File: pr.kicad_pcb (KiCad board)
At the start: 2 copper layers, 65 x 86 mm, 42 parts, among them P1 CONN_01X02, P2 CONN_01X02, P4 BDM, P5 CONN_01X03, P6 CONN_01X02, T1 TRANSFO, U1 78L05, U2 MC9S08SH8, U4 LM311N, U5 SSR_SHARP

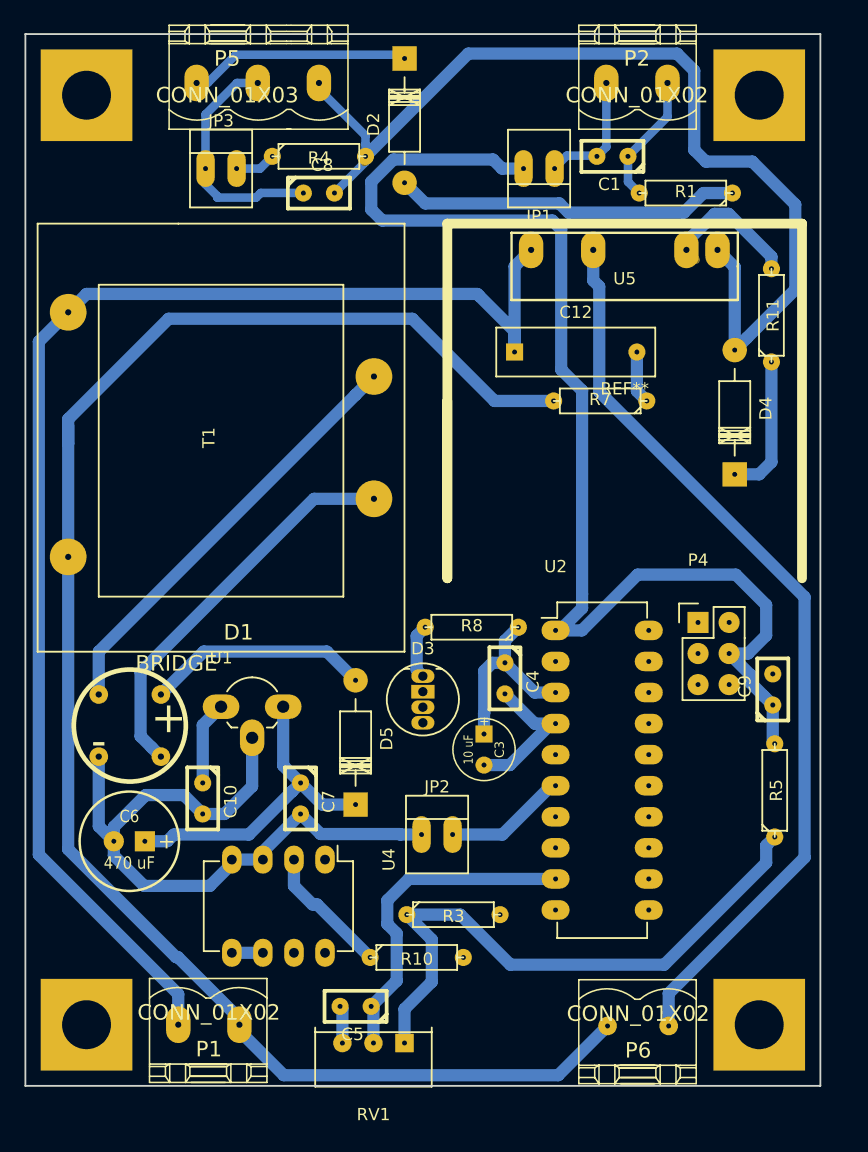
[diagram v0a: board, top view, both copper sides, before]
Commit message: modificado componente ruteado
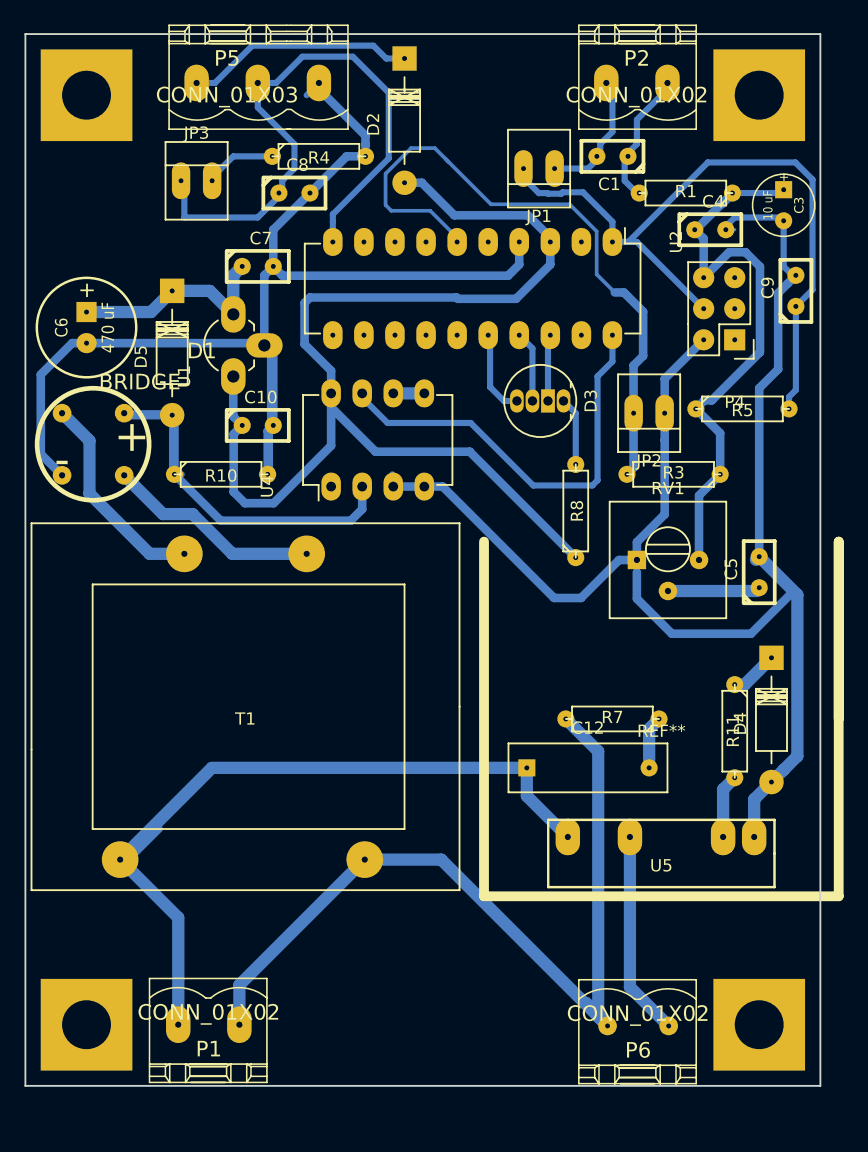
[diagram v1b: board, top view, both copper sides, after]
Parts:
- RV1: footprint Potentiometers:Potentiometer_Trimmer-Suntan-TSR-3386C -> Potentiometers:Potentiometer_Trimmer-Suntan-TSR-3386P
- moved C3 50.8 mm to (106.0, 64.0)
- moved C5 48.5 mm to (104.0, 94.0), turned to 90 degrees
- moved U5 48.1 mm to (96.0, 117.0)
- moved D5 44.6 mm to (56.0, 71.0), turned to 270 degrees
- moved RV1 43.8 mm to (94.0, 93.0), turned to 0 degrees
- moved C7 43.6 mm to (63.0, 69.0), turned to 0 degrees
- moved R10 42.6 mm to (60.0, 86.0)
- moved C6 42.1 mm to (49.0, 74.0), turned to 270 degrees
- moved C4 40.3 mm to (100.0, 66.0), turned to 0 degrees
- moved R3 40.2 mm to (97.0, 86.0), turned to 180 degrees
- moved JP2 38.6 mm to (95.0, 81.0), turned to 180 degrees
- moved R11 34.1 mm to (102.0, 107.0), turned to 270 degrees
- moved C12 34.0 mm to (85.0, 110.0)
- moved C9 32.6 mm to (107.0, 71.0)
- moved U2 32.1 mm to (92.0, 67.0), turned to 270 degrees
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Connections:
- RV1 pad 1: /vreg -> GND
- RV1 pad 3: GND -> /vreg
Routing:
- net GND: track 155.9 -> 234.7 mm
- net /L: track 141.9 -> 65.7 mm
- net /N: track 136.5 -> 75.1 mm
- net Net-(P6-Pad1): track 75.3 -> 16.8 mm
- net /vreg: track 100.2 -> 146.7 mm
- net Net-(JP2-Pad2): track 10.1 -> 53.9 mm
- net /RESET: track 101.8 -> 61.4 mm
- net /ZC: track 0.35 -> 35.1 mm
- net Net-(C8-Pad1): track 19.9 -> 50.2 mm
- net /ST: track 27.4 -> 7.57 mm
- net Net-(D1-Pad2): track 35.3 -> 17.3 mm
- net Net-(D1-Pad4): track 32.5 -> 17.6 mm
- net /IZC: track 29.1 -> 38.8 mm
- net Net-(C6-Pad1): track 26.8 -> 17.7 mm
- net Net-(R11-Pad2): track 12.6 -> 5.23 mm
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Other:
- net class Default: trace_width 1 -> 0.7
- net class PW added: clearance 0.4, trace_width 0.7, via_dia 0.6, via_drill 0.4

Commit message: prototipo1.0 enviado a fabricar
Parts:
- added G***: LOGO, locales:LOGO, B.Cu at (76.0, 128.2)
- moved RV1 4.50 mm to (93.6, 97.5)
- moved D2 2.68 mm to (77.7, 52.0)
- moved R8 2.41 mm to (88.8, 91.4)
- moved REF** 1.61 mm to (94.5, 105.5)
- moved U5 1.52 mm to (94.5, 116.8)
- moved C8 1.42 mm to (67.1, 62.1)
- moved R5 1.14 mm to (103.8, 80.8)
- moved C6 1.02 mm to (50.0, 74.0)
- moved R4 0.81 mm to (67.9, 59.2)
- moved JP3 0.77 mm to (58.4, 61.4)
- moved D1 0.75 mm to (47.8, 81.0)
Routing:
- net /ST: track 7.57 -> 128.8 mm, vias 0 -> 4
- net /AcOut: track 5.10 -> 75.4 mm, vias 0 -> 2
- net /vreg: track 146.7 -> 176.5 mm, vias 0 -> 2
- net /BDM: track 0.03 -> 26.4 mm, vias 0 -> 2
- net GND: track 234.7 -> 260.0 mm, vias 0 -> 2
- net Net-(JP2-Pad2): track 53.9 -> 65.3 mm
- net /ZC: track 35.1 -> 43.9 mm
- net /L: track 65.7 -> 60.9 mm
- net Net-(D2-Pad1): track 18.7 -> 22.9 mm
- net Net-(C8-Pad1): track 50.2 -> 47.0 mm
- net Net-(D3-Pad1): track 5.60 -> 7.95 mm
- net Net-(R11-Pad2): track 5.23 -> 6.99 mm
- net /IZC: track 38.8 -> 39.9 mm
- net Net-(JP3-Pad2): track 6.29 -> 5.24 mm
- net Net-(C6-Pad1): track 17.7 -> 16.7 mm
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- added copper zone on B.Cu, net GND
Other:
- net class Default: trace_width 0.7 -> 1; via_dia 0.6 -> 1.5
- net class PW: trace_width 0.7 -> 1; via_dia 0.6 -> 1.5
- rule trace_min: 0.2 -> 0.3

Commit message: realizando firmware
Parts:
- removed JP1: JUMPER, Connect:PINHEAD1-2
- added R12: 1M, Discret:R3, F.Cu at (83.6, 90.3)
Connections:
- C1 pad 1: /GP -> /RESET
- C1 pad 2: Net-(C1-Pad2) -> GND
- P2 pad 1: Net-(C1-Pad2) -> GND
- P2 pad 2: /GP -> /RESET
- R1 pad 2: /GP -> /RESET
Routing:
- net GND: track 260.0 -> 288.0 mm, vias 2 -> 4
- net /GP: track 12.3 -> 0.00 mm
- net Net-(C1-Pad2): track 11.6 -> 0.00 mm
- net /RESET: track 61.1 -> 63.8 mm
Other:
- net class Default: trace_width 1 -> 0.5
